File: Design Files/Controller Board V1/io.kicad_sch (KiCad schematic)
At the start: 6 parts, among them J1 XT30PW-M, J2 XT30PW-M, J3 XT30PW-M, J4 XT30PW-M, J5 XT30PW-M, J6 XT30PW-M

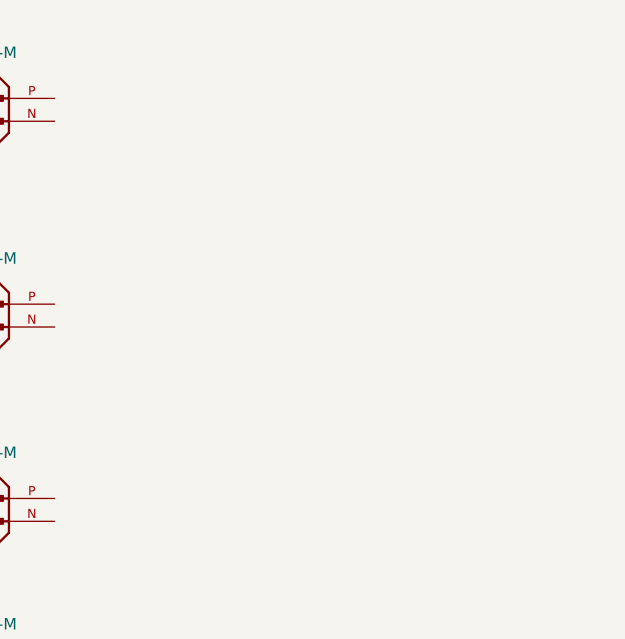
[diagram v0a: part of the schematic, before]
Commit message: Added jst 4 pin connector
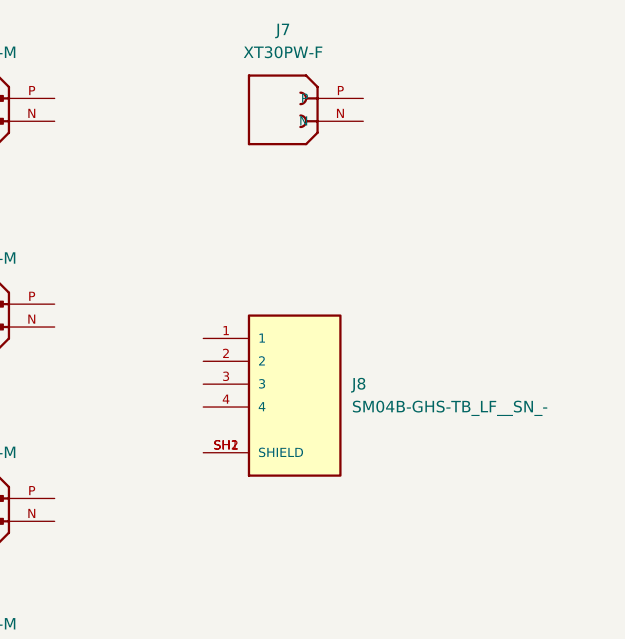
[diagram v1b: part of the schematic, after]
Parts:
- added J7: XT30PW-F, XT30PW-F:AMASS_XT30PW-F, symbol XT30PW-F:XT30PW-F
- added J8: SM04B-GHS-TB_LF__SN_-, SM04B-GHS-TB_LF__SN_-:JST_SM04B-GHS-TB_LF__SN_-, symbol SM04B-GHS-TB_LF__SN_-:SM04B-GHS-TB_LF__SN_-
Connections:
- new net: J8.SH1 (SHIELD), J8.SH2 (SHIELD)

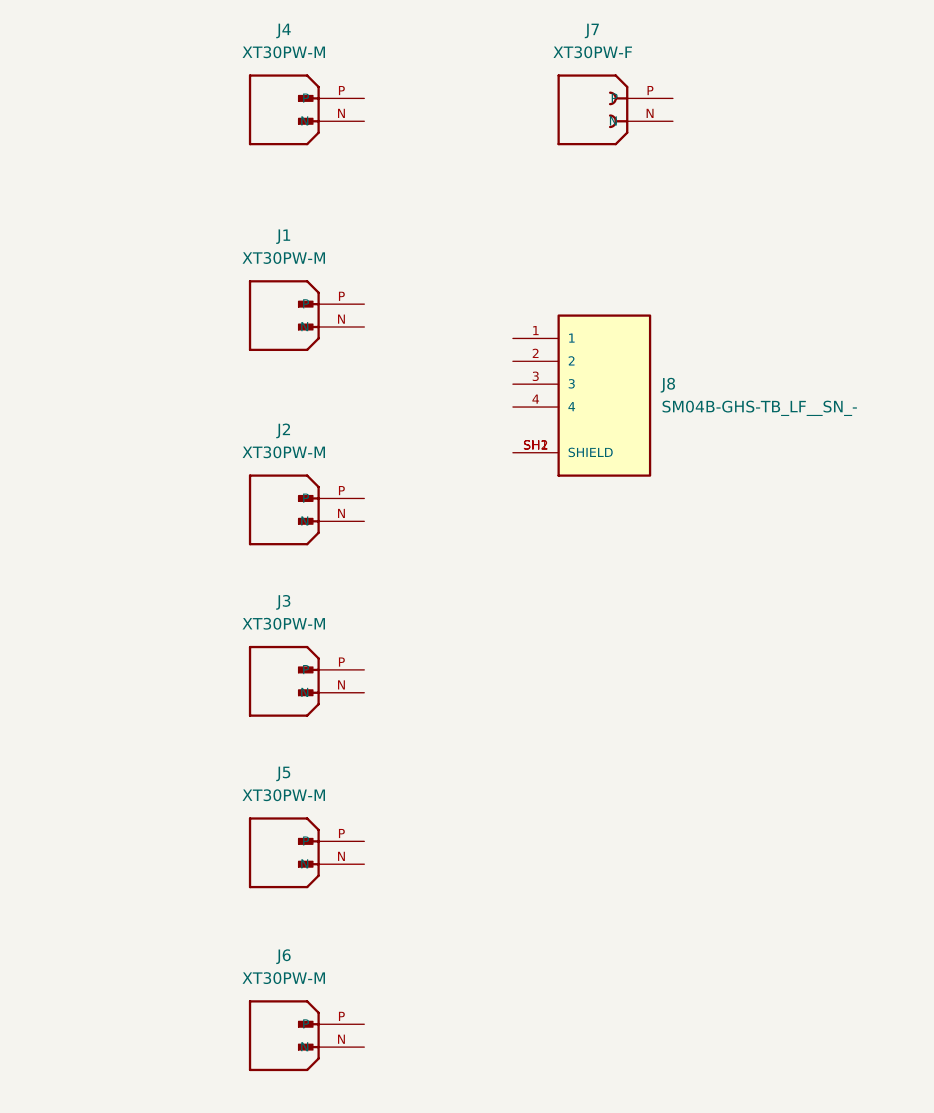
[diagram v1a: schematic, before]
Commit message: Edited XT30 symbols to include solder points
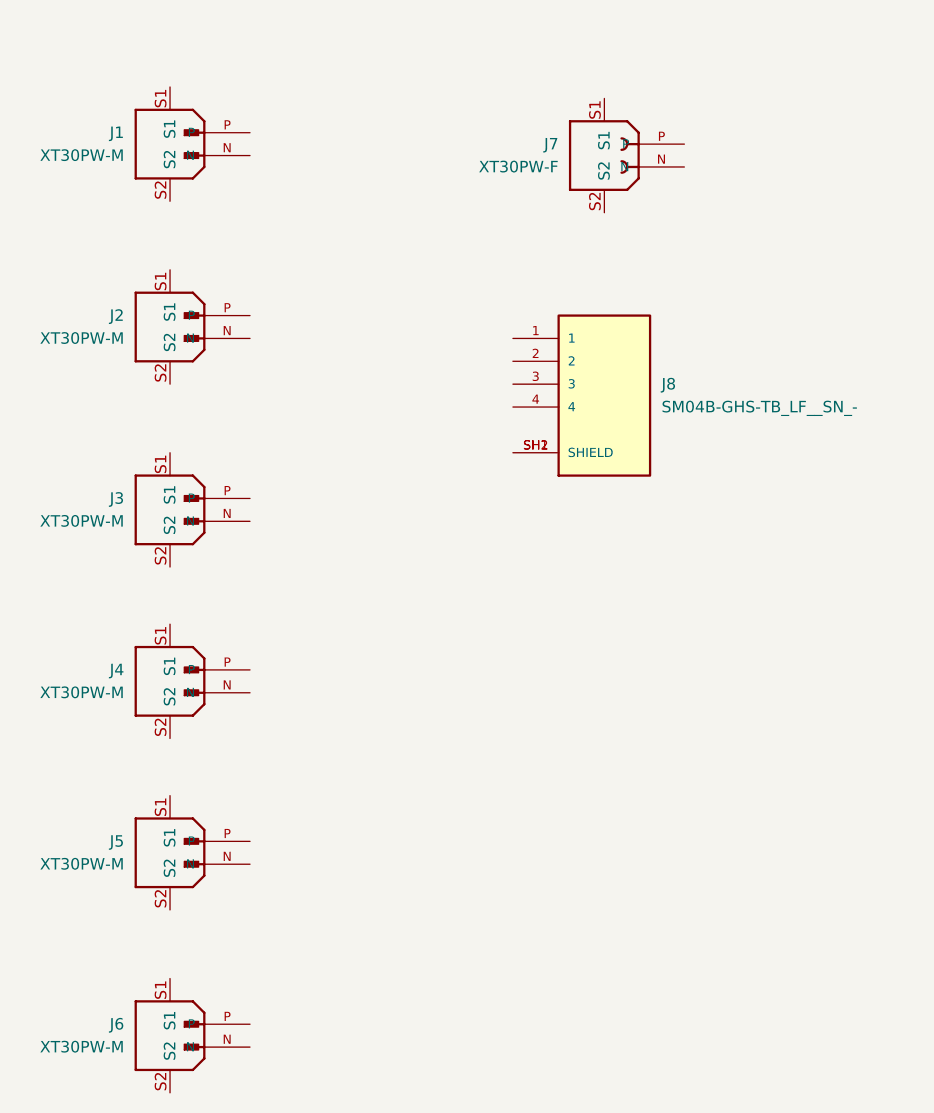
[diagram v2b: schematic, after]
